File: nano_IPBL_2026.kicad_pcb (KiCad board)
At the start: 2 copper layers, 44 x 85 mm, 22 parts, among them J3 DB301V-5.0-2P, M1 Motor_Servo, M10 Motor_Servo, M11 Motor_Servo, M12 Motor_Servo, M2 Motor_Servo, M3 Motor_Servo, M4 Motor_Servo, M5 Motor_Servo, M6 Motor_Servo, M7 Motor_Servo, M8 Motor_Servo, M9 Motor_Servo, SW1 SW_DPDT_x2, U1 LM1085-5.0, U2 LM1085-5.0

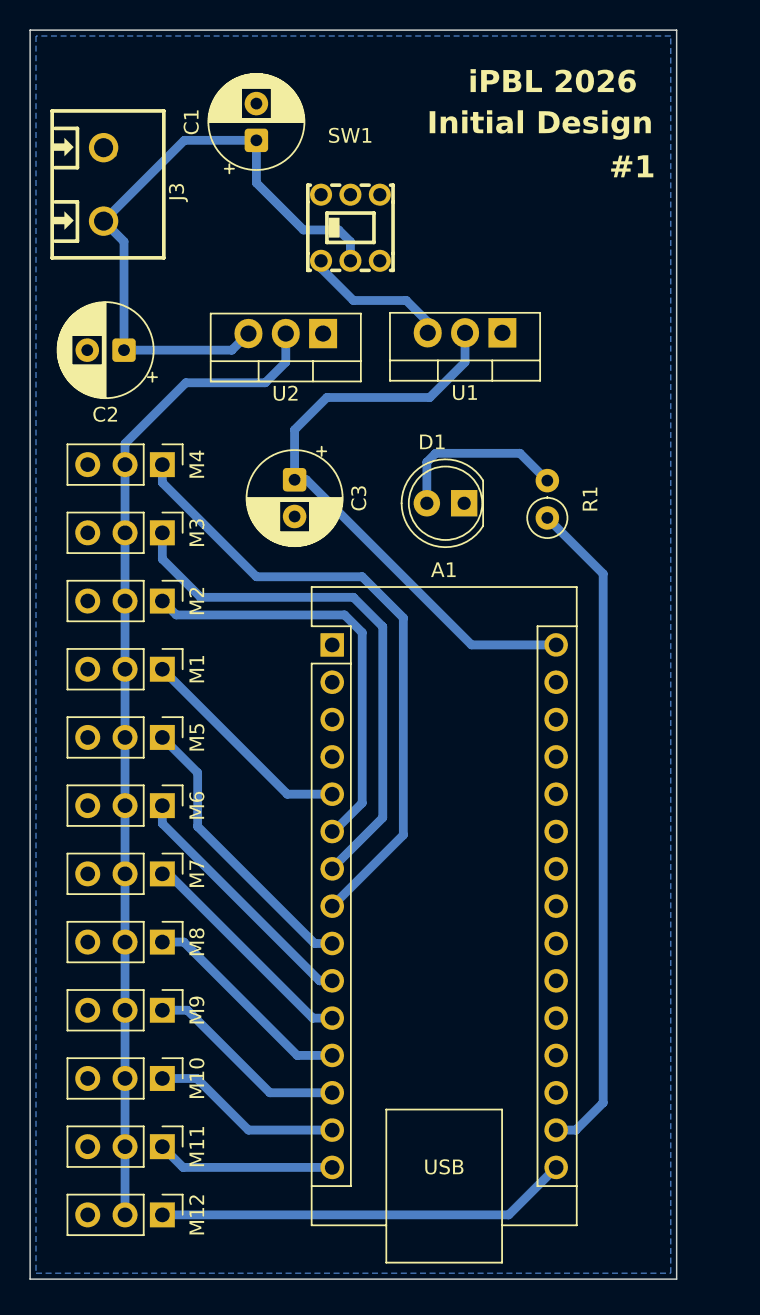
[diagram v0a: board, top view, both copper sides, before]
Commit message: Changed padding drill sizes and exported copper layer as SVG
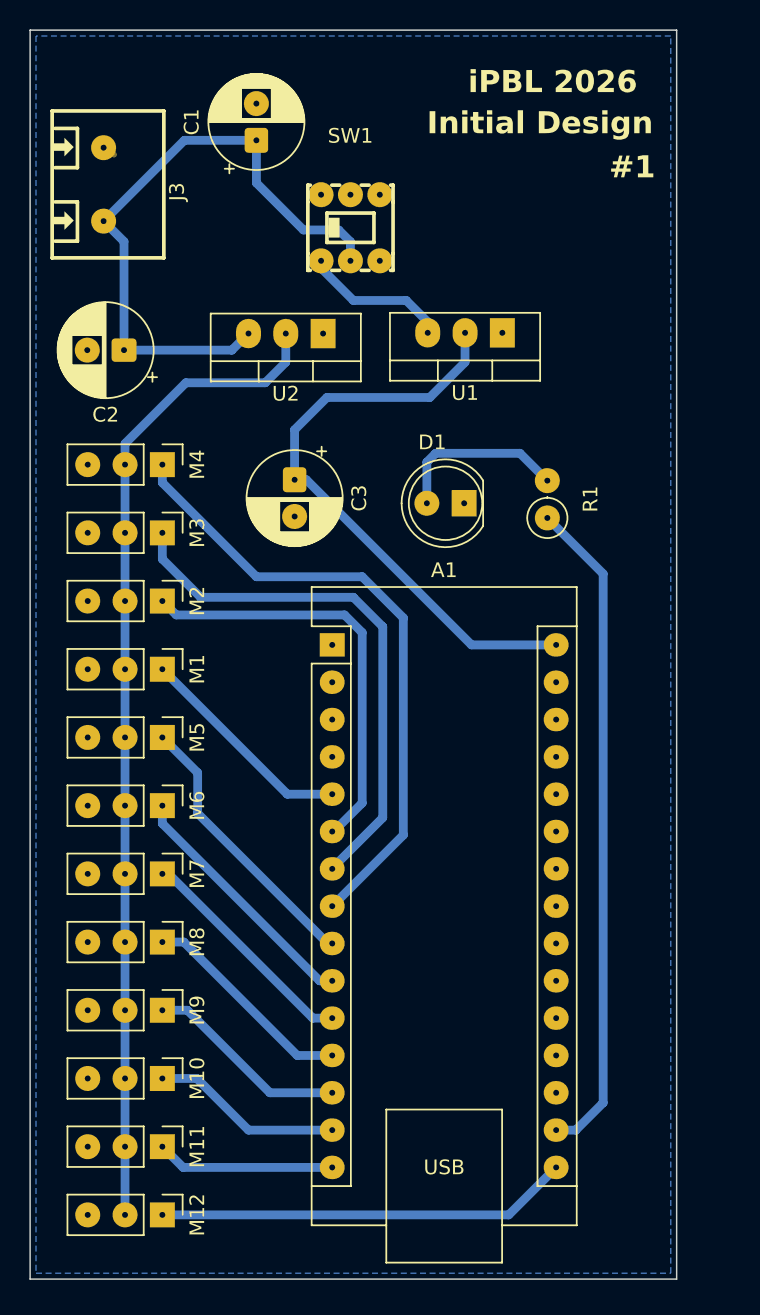
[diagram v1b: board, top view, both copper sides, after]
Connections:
- net Net-(J3-Pin_2) renamed VCC
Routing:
- net Net-(A1-D6): track 19.5 -> 19.0 mm

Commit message: Refine PCB design and power circuit
- Fix switch connection to come before voltage regulator (stepdown)
- Increase via diameter to 1mm for better current distribution
- Add 0.25mm copper pad diameter with 0.4mm drill holes
- Rearrange component placement for improved PCB layout
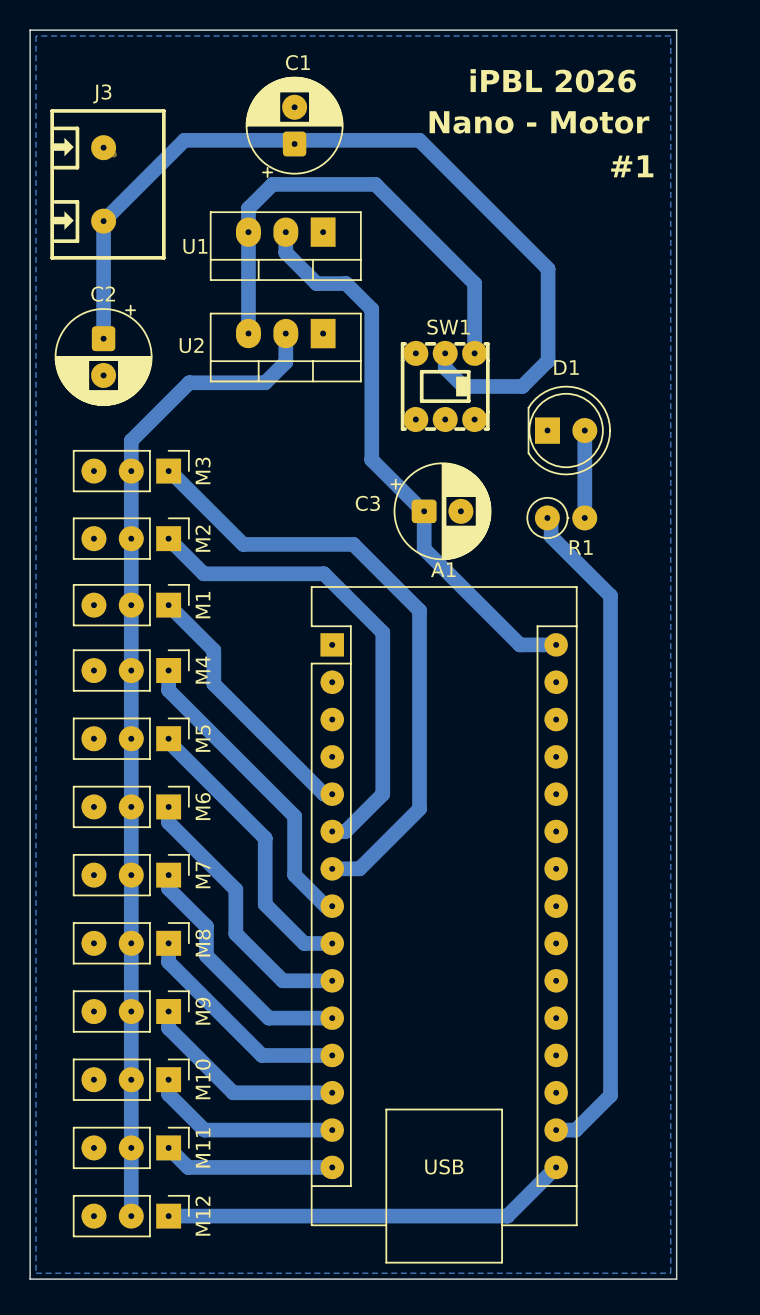
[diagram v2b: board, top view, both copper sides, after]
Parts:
- moved M4 14.0 mm to (112.4, 93.6)
- moved U1 14.0 mm to (122.9, 63.8)
- moved SW1 12.6 mm to (131.2, 74.2), turned to 180 degrees
- moved C3 9.08 mm to (129.8, 82.8), turned to 0 degrees
- moved D1 7.53 mm to (138.2, 77.2), turned to 0 degrees
- moved M1 4.38 mm to (112.4, 89.1)
- moved M2 4.27 mm to (112.4, 84.6)
- moved M3 4.22 mm to (112.4, 80.0)
- moved C1 2.61 mm to (121.0, 57.8)
- moved C2 1.59 mm to (108.0, 71.0), turned to -90 degrees
- moved M5 0.43 mm to (112.4, 98.2)
- moved M6 0.43 mm to (112.4, 102.9)
- moved M7 0.43 mm to (112.4, 107.5)
- moved M8 0.43 mm to (112.4, 112.1)
- moved M9 0.43 mm to (112.4, 116.8)
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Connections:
- U2 pad 3: VCC -> Net-(SW1A-A)
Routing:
- net Net-(A1-D5): track 43.1 -> 20.9 mm
- net Net-(SW1A-A): track 10.0 -> 32.1 mm
- net VCC: track 43.5 -> 59.9 mm
- net Net-(D1-A): track 12.0 -> 5.95 mm
- net Net-(A1-D4): track 36.6 -> 42.1 mm
- net Net-(A1-D3): track 28.9 -> 32.7 mm
- net Net-(A1-VIN): track 41.4 -> 38.5 mm
- net Net-(A1-D2): track 15.1 -> 17.8 mm
- net Net-(A1-D8): track 15.6 -> 16.9 mm
- net Net-(A1-D7): track 17.2 -> 18.4 mm
- net Net-(A1-D6): track 19.0 -> 19.7 mm
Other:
- board text added: "Nano - Motor"
- board text removed: "Initial Design"

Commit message: Remove step-down regulator and switch, add RX/TX mounting pads
Replace the switch with a mounting pad, remove the step-down regulator,
and add mounting pad connections for RX/TX. Reposition components to
fit the actual enclosure, and move the 100uF capacitor closer to the Nano.
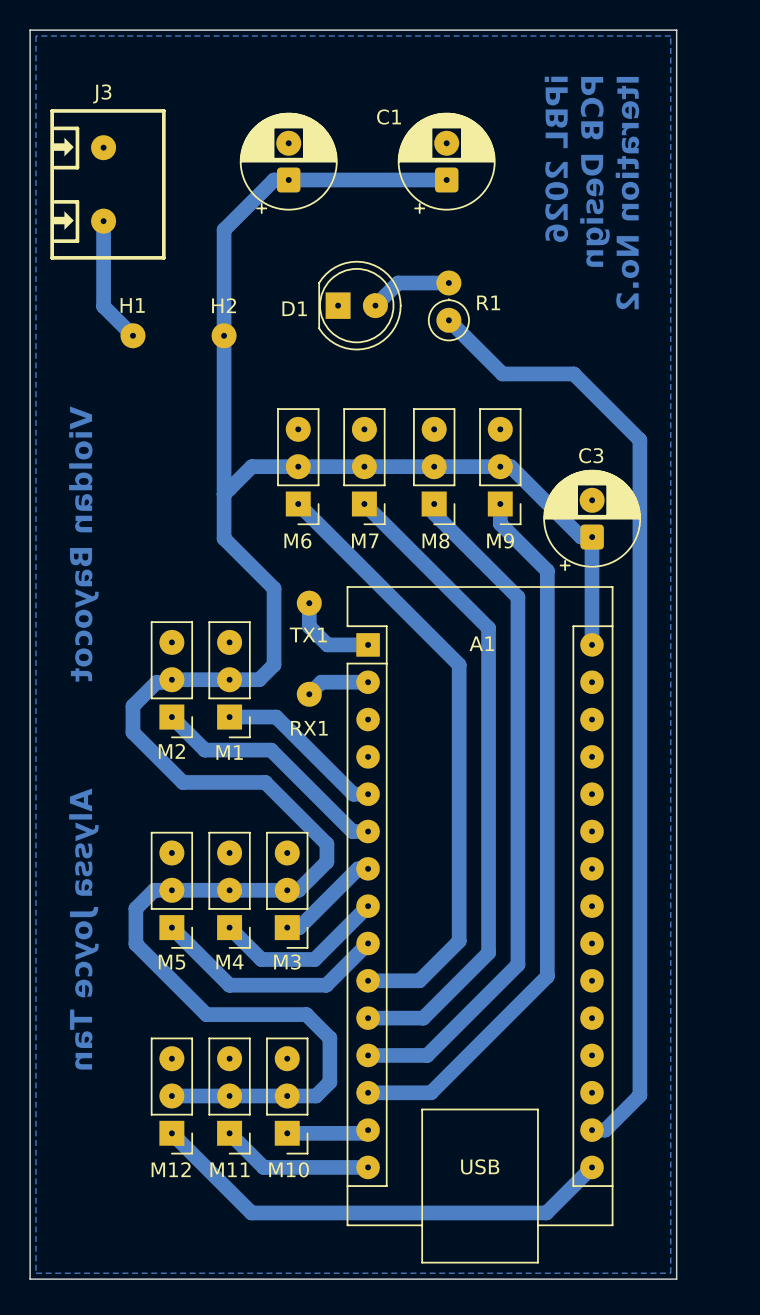
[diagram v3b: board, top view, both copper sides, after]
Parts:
- removed SW1: SW_DPDT_x2, lcsc:SW-TH_6P-L5.8-W5.8-P2.00-LS4.5-BL_1
- removed U1, U2: LM1085-5.0, Package_TO_SOT_THT:TO-220-3_Vertical
- added H1: MountingHole_Pad, Arduino_MountingHole:MountingHole_1.2mm_M2_Pad_EDITED, F.Cu at (110.0, 70.8)
- added H2: MountingHole_Pad, Arduino_MountingHole:MountingHole_1.2mm_M2_Pad_EDITED, F.Cu at (116.2, 70.8)
- added RX1: MountingHole_Pad, Arduino_MountingHole:MountingHole_1.2mm_M2_Pad_EDITED, F.Cu at (122.0, 95.2)
- added TX1: MountingHole_Pad, Arduino_MountingHole:MountingHole_1.2mm_M2_Pad_EDITED, F.Cu at (122.0, 89.0)
- moved M9 41.3 mm to (135.0, 82.2), turned to 180 degrees
- moved M8 34.9 mm to (130.5, 82.2), turned to 180 degrees
- moved M3 32.1 mm to (120.5, 111.1), turned to 180 degrees
- moved M7 28.6 mm to (125.8, 82.2), turned to 180 degrees
- moved M6 22.4 mm to (121.2, 82.2), turned to 180 degrees
- moved M4 18.0 mm to (116.6, 111.1), turned to 180 degrees
- moved C2 16.6 mm to (120.6, 60.2), turned to 90 degrees
- moved D1 16.6 mm to (124.0, 68.8)
- moved R1 15.0 mm to (131.5, 69.8), turned to 90 degrees
- moved M5 12.9 mm to (112.6, 111.1), turned to 180 degrees
- moved M2 12.1 mm to (112.6, 96.8), turned to 180 degrees
- moved C3 11.6 mm to (141.2, 84.5), turned to 90 degrees
- moved C1 10.6 mm to (131.3, 60.2)
- moved M10 8.86 mm to (120.5, 125.1), turned to 180 degrees
- moved M1 8.67 mm to (116.6, 96.8), turned to 180 degrees
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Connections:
- A1 pad 1: unconnected-(A1-D1/TX-Pad1) -> Net-(A1-D1/TX)
- A1 pad 2: unconnected-(A1-D0/RX-Pad2) -> Net-(A1-D0/RX)
- C1 pad 1: VCC -> Net-(A1-VIN)
- C2 pad 1: VCC -> Net-(A1-VIN)
- M1 pad 2: Net-(M1-+) -> Net-(A1-VIN)
- M10 pad 2: Net-(M1-+) -> Net-(A1-VIN)
- M11 pad 2: Net-(M1-+) -> Net-(A1-VIN)
- M12 pad 2: Net-(M1-+) -> Net-(A1-VIN)
- M2 pad 2: Net-(M1-+) -> Net-(A1-VIN)
- M3 pad 2: Net-(M1-+) -> Net-(A1-VIN)
- M4 pad 2: Net-(M1-+) -> Net-(A1-VIN)
- M5 pad 2: Net-(M1-+) -> Net-(A1-VIN)
- M6 pad 2: Net-(M1-+) -> Net-(A1-VIN)
- M7 pad 2: Net-(M1-+) -> Net-(A1-VIN)
- M8 pad 2: Net-(M1-+) -> Net-(A1-VIN)
- M9 pad 2: Net-(M1-+) -> Net-(A1-VIN)
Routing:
- net Net-(A1-VIN): track 38.5 -> 159.5 mm
- net Net-(M1-+): track 67.4 -> 0.00 mm
- net VCC: track 59.9 -> 8.63 mm
- net Net-(A1-D4): track 42.1 -> 7.16 mm
- net Net-(A1-D10): track 14.1 -> 49.0 mm
- net Net-(SW1A-A): track 32.1 -> 0.00 mm
- net Net-(A1-D9): track 15.0 -> 46.5 mm
- net Net-(A1-D8): track 16.9 -> 44.1 mm
- net Net-(A1-D7): track 18.4 -> 41.6 mm
- net Net-(A1-3V3): track 45.7 -> 65.2 mm
- net Net-(A1-D3): track 32.7 -> 16.6 mm
- net Net-(A1-D5): track 20.9 -> 11.8 mm
- net Net-(A1-D11): track 13.1 -> 5.59 mm
- net Net-(A1-D2): track 17.8 -> 11.6 mm
- net Net-(A1-D1/TX): track 0.00 -> 6.11 mm
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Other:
- board text added: "Alyssa Joyce Tan"
- board text added: "Violdan Bayocot"
- board text added: "iPBL 2026 PCB Design Iteration No.2"
- board text removed: "#1"
- board text removed: "Nano - Motor"
- board text removed: "iPBL 2026"

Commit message: Adjust track width and copper clearance, match solder mask to copper pad width
Update silkscreen text and drill hole visibility on B_Cu/F_Silkscreen layers.
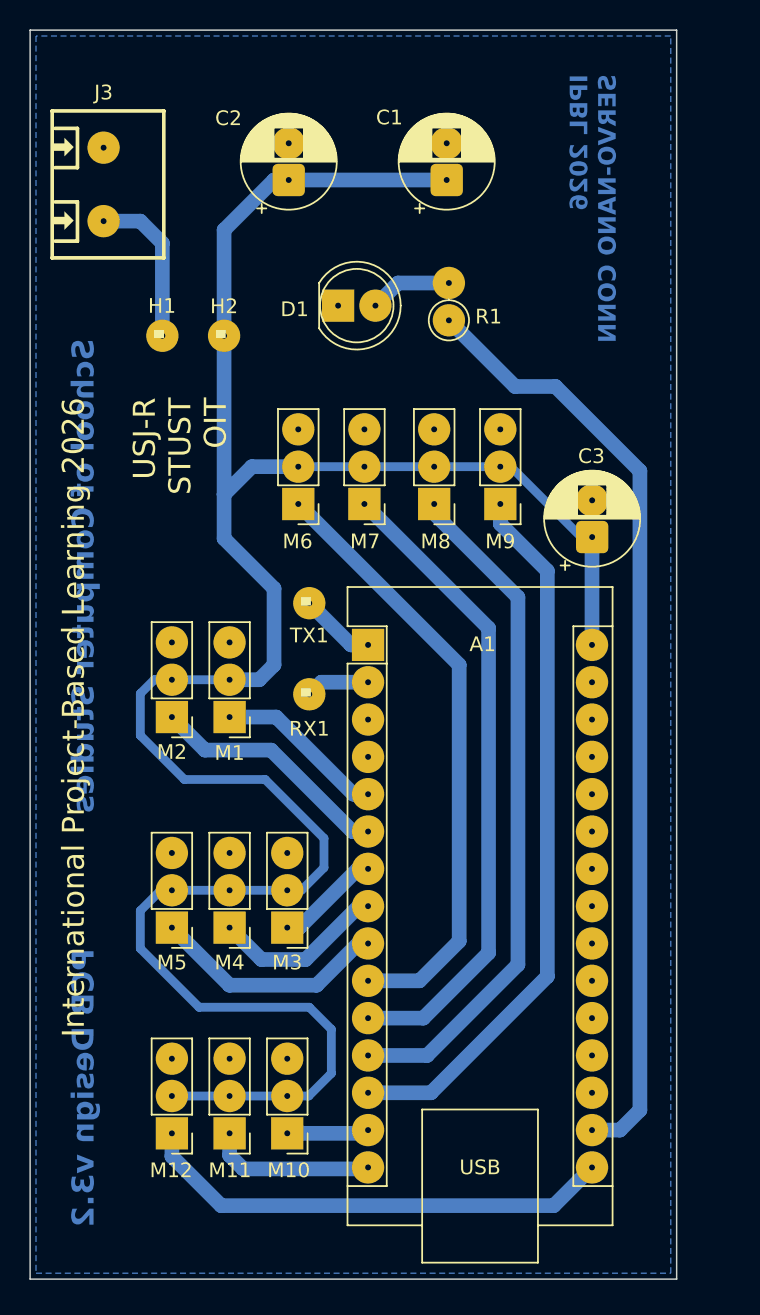
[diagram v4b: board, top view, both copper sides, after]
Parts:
- moved H1 2.00 mm to (112.0, 70.8)
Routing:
- net VCC: track 8.63 -> 10.9 mm
- net Net-(A1-D12): track 10.4 -> 11.3 mm
- net Net-(A1-D1/TX): track 6.11 -> 5.18 mm
- net Net-(A1-3V3): track 65.2 -> 64.6 mm
- net Net-(A1-D13): track 32.1 -> 32.6 mm
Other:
- board text added: "."
- board text added: "IPBL 2026 SERVO-NANO CONN"
- board text added: "International Project-Based Learning 2026 USJ-R STUST OIT"
- board text added: "PCB Design v3.2"
- board text added: "School of Computer Studies"
- board text removed: "Alyssa Joyce Tan"
- board text removed: "Violdan Bayocot"
- board text removed: "iPBL 2026 PCB Design Iteration No.2"
